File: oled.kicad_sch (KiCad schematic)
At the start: 23 parts, among them Q3 IRLML6402, Q4 BSS138, Q5 BSS138, U7 AP3012KTR-E1

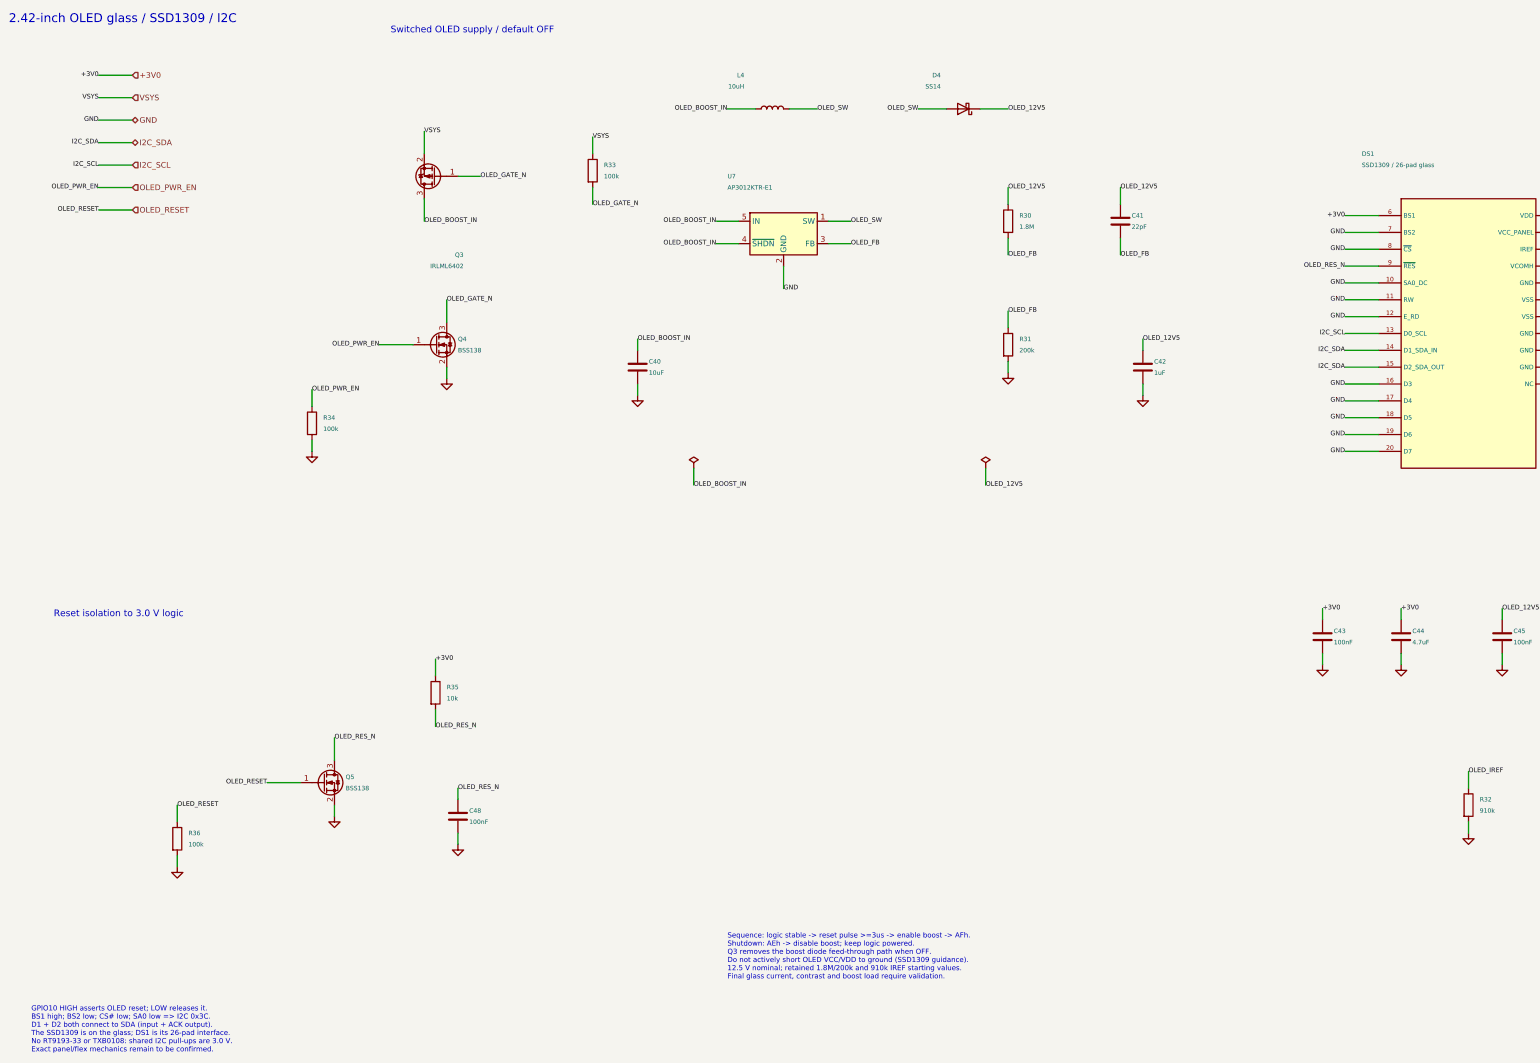
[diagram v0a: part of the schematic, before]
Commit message: Add PCB NFC coil and refine prototype component selections
Integrate a reusable 40 mm four-turn antenna footprint, calculated matching
network, hand-solder tuning pads, and a fabrication-ready bare-coil coupon.
Archive RF calculations, simulation results, reference sources, and tuning
instructions.

Select the PN7160 crystal and supply capacitors using manufacturer guidance
and DC-bias data. Record the confirmed 26-contact OLED interface and dedicated
5 V / 1.5 A USB-C source, retaining the JST-PH battery connector and deferred
battery behavior. Update the BOM, schematic PDFs, and verification tools.

Validation: native KiCad ERC reports zero violations; all current schematic
hashes match the verification report. Coil geometry, coupon DRC, RF model,
and component calculation results are archived with the design.
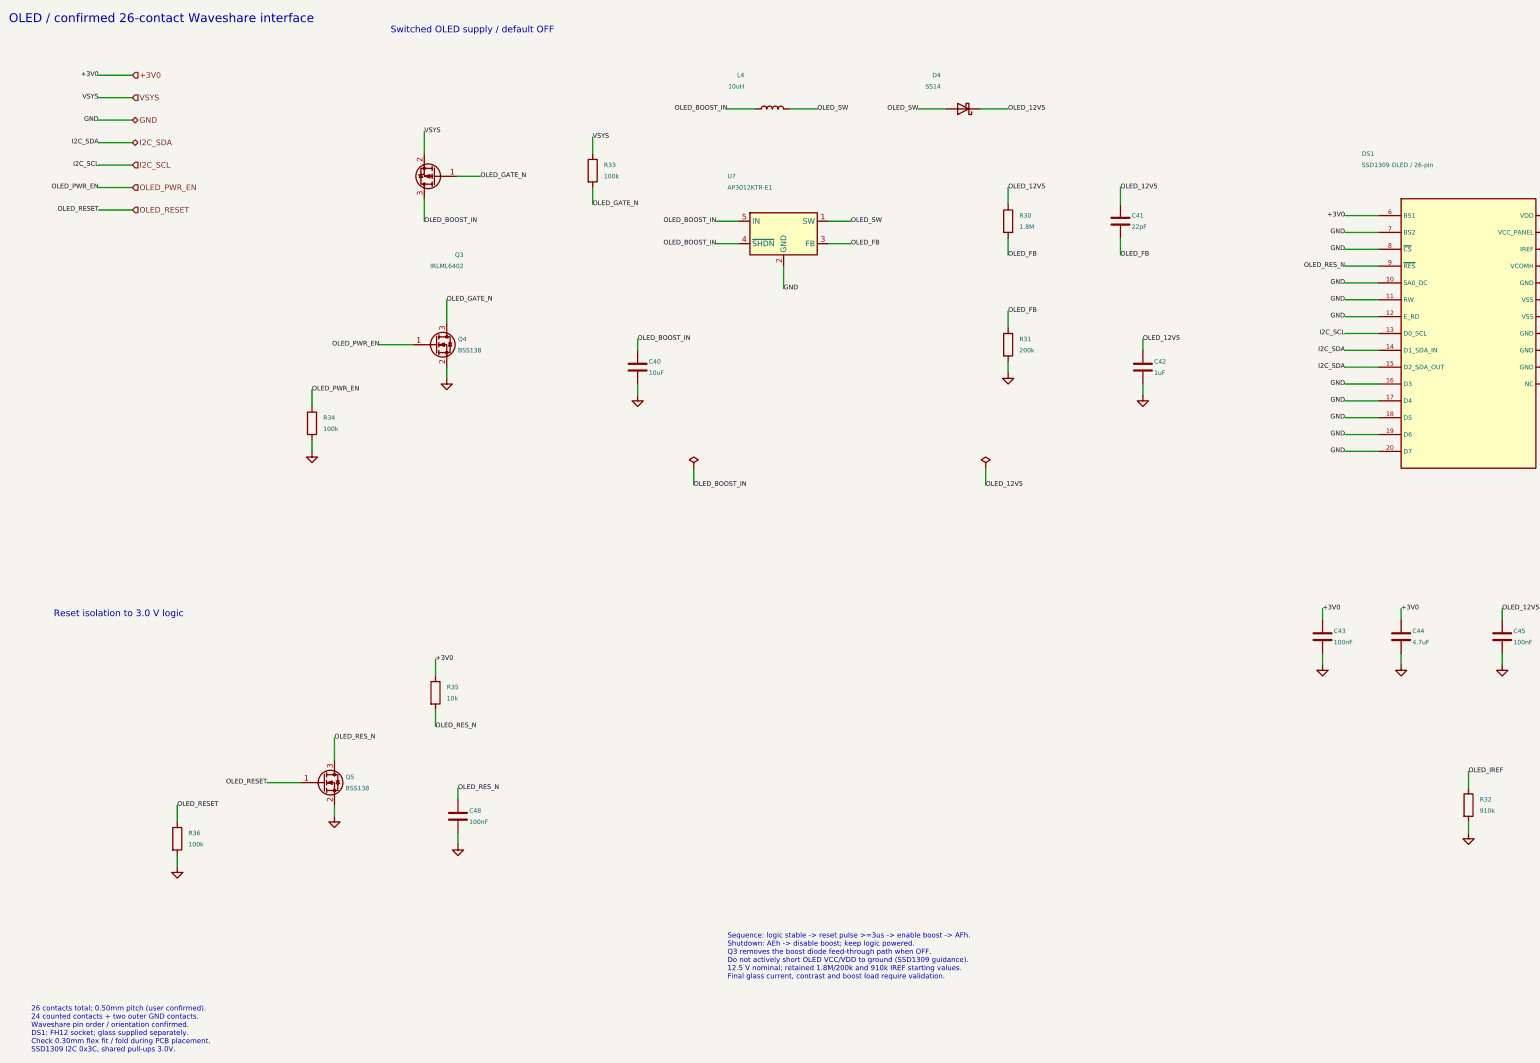
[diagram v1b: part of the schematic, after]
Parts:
- C40: footprint Capacitor_SMD:C_0805_2012Metric -> Capacitor_SMD:C_1206_3216Metric; LCSC (none) -> C14860; MPN (none) -> CL31B106KAHNNNE; Manufacturer (none) -> Samsung Electro-Mechanics; Tolerance 20% -> 10%; Voltage 10 V -> 25 V
- C42: LCSC (none) -> C28323; MPN (none) -> CL21B105KBFNNNE; Manufacturer (none) -> Samsung Electro-Mechanics; Tolerance 20% -> 10%; Voltage 25 V -> 50 V
- C44: LCSC (none) -> C98195; MPN (none) -> CL21B475KAFNNNE; Manufacturer (none) -> Samsung Electro-Mechanics; Tolerance 20% -> 10%; Voltage 10 V -> 25 V
- C46: footprint Capacitor_SMD:C_0805_2012Metric -> Capacitor_SMD:C_1206_3216Metric; LCSC (none) -> C51205; MPN (none) -> CL31B475KBHNNNE; Manufacturer (none) -> Samsung Electro-Mechanics; Tolerance 20% -> 10%; Voltage 25 V -> 50 V
- C47: LCSC (none) -> C19110; MPN (none) -> CL21B225KAFNNNE; Manufacturer (none) -> Samsung Electro-Mechanics; Tolerance 20% -> 10%
- DS1: value SSD1309 / 26-pad glass -> SSD1309 OLED / 26-pin; Actual Flex (none) -> 26 contacts total: 24 counted plus two outer GND contacts; 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; Connector Datasheet (none) -> https://www.hirose.com/product/p/CL0586-0576-2-55; Connector Mechanics (none) -> FH12 bottom-contact, 0.30 mm flex thickness; check insertio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; Footprint Status PROVISIONAL: confirm 26-pin 0.5 mm flex/contact side; may r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 -> SELECTED: 26-way 0.50 mm; user confirms Waveshare pin order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; MPN TBD exact OLED glass -> FH12-26S-0.5SH(55); Manufacturer (none) -> Hirose; Status (none) -> Pinout/orientation confirmed by user; DS1 BOM part is the F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
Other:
- note added: "26 contacts total; 0.50mm pitch (user confirmed). 24 counted contacts + two outer GND contacts. Waveshare pin order / orientation confirmed. DS1: FH12 socket; glass supplied separately. Check 0.30mm flex fit / fold during PCB placement. SSD1309 I2C 0x3C, shared pull-ups 3.0V."
- note added: "OLED / confirmed 26-contact Waveshare interface"
- note removed: "2.42-inch OLED glass / SSD1309 / I2C"
- note removed: "GPIO10 HIGH asserts OLED reset; LOW releases it. BS1 high; BS2 low; CS# low; SA0 low => I2C 0x3C. D1 + D2 both connect to SDA (input + ACK output). The SSD1309 is on the glass; DS1 is its 26-pad interface. No RT9193-33 or TXB0108: shared I2C pull-ups are 3.0 V. Exact panel/flex mechanics remain to be confirmed."
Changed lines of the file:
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@@
     (rev "B-draft")
   )
-  (text "2.42-inch OLED glass / SSD1309 / I2C"
+  (text "OLED / confirmed 26-contact Waveshare interface"
     (at 15.24 17.78 0)
     (effects
@@
       )
     )
-    (property "Footprint" "Capacitor_SMD:C_0805_2012Metric"
+    (property "Footprint" "Capacitor_SMD:C_1206_3216Metric"
       (at 157.48 96.52 0)
       (effects
@@
       )
     )
-    (property "Datasheet" ""
+    (property "Datasheet" "https://product.samsungsem.com/mlcc/CL31B106KAHNNN.do"
       (at 157.48 96.52 0)
       (effects
@@
       )
     )
-    (property "Voltage" "10 V"
+    (property "Voltage" "25 V"
       (at 157.48 96.52 0)
       (effects
@@
       )
     )
-    (property "Tolerance" "20%"
+    (property "Tolerance" "10%"
       (at 157.48 96.52 0)
       (effects
@@
       )
     )
+    (property "Manufacturer" "Samsung Electro-Mechanics"
+      (at 157.48 96.52 0)
+      (effects
+        (font
+          (size 1.27 1.27)
+        )
+        (hide yes)
+      )
+    )
+    (property "MPN" "CL31B106KAHNNNE"
+      (at 157.48 96.52 0)
+      (effects
+        (font
+          (size 1.27 1.27)
+        )
+        (hide yes)
+      )
+    )
+    (property "LCSC" "C14860"
+      (at 157.48 96.52 0)
+      (effects
+        (font
+          (size 1.27 1.27)
+        )
+        (hide yes)
+      )
+    )
     (pin "1"
     )
@@
       )
     )
-    (property "Datasheet" ""
+    (property "Datasheet" "https://product.samsungsem.com/mlcc/CL21B105KBFNNN.do"
       (at 271.78 96.52 0)
       (effects
@@
       )
     )
-    (property "Voltage" "25 V"
+    (property "Voltage" "50 V"
       (at 271.78 96.52 0)
       (effects
@@
       )
     )
-    (property "Tolerance" "20%"
+    (property "Tolerance" "10%"
       (at 271.78 96.52 0)
       (effects
@@
       )
     )
+    (property "Manufacturer" "Samsung Electro-Mechanics"
+      (at 271.78 96.52 0)
+      (effects
+        (font
+          (size 1.27 1.27)
+        )
+        (hide yes)
+      )
+    )
+    (property "MPN" "CL21B105KBFNNNE"
+      (at 271.78 96.52 0)
+      (effects
+        (font
+          (size 1.27 1.27)
+        )
+        (hide yes)
+      )
+    )
+    (property "LCSC" "C28323"
+      (at 271.78 96.52 0)
+      (effects
+        (font
+          (size 1.27 1.27)
+        )
+        (hide yes)
+      )
+    )
     (pin "1"
     )
@@
       )
     )
-    (property "Value" "SSD1309 / 26-pad glass"
+    (property "Value" "SSD1309 OLED / 26-pin"
       (at 321.31 50.8 0)
       (effects
@@
       )
     )
-    (property "MPN" "TBD exact OLED glass"
+    (property "MPN" "FH12-26S-0.5SH(55)"
       (at 345.44 88.9 0)
       (effects
@@
       )
     )
-    (property "Footprint Status" "PROVISIONAL: confirm 26-pin 0.5 mm flex/contact side; may require solder pads instead"
+    (property "Footprint Status" "SELECTED: 26-way 0.50 mm; user confirms Waveshare pin order/orientation, including outer ground contacts"
       (at 345.44 88.9 0)
       (effects
@@
       )
     )
+    (property "Actual Flex" "26 contacts total: 24 counted plus two outer GND contacts; 0.50 mm pitch; copper on emitting side (user confirmed)"
+      (at 345.44 88.9 0)
+      (effects
+        (font
+          (size 1.27 1.27)
+        )
+        (hide yes)
+      )
+    )
+    (property "Status" "Pinout/orientation confirmed by user; DS1 BOM part is the FPC socket, OLED glass supplied separately"
+      (at 345.44 88.9 0)
+      (effects
+        (font
+          (size 1.27 1.27)
+        )
+        (hide yes)
+      )
+    )
+    (property "Manufacturer" "Hirose"
+      (at 345.44 88.9 0)
+      (effects
+        (font
+          (size 1.27 1.27)
+        )
+        (hide yes)
+      )
+    )
+    (property "Connector Mechanics" "FH12 bottom-contact, 0.30 mm flex thickness; check insertion/fold and physical fit during PCB placement"
+      (at 345.44 88.9 0)
+      (effects
+        (font
+          (size 1.27 1.27)
+        )
+        (hide yes)
+      )
+    )
+    (property "Connector Datasheet" "https://www.hirose.com/product/p/CL0586-0576-2-55"
+      (at 345.44 88.9 0)
+      (effects
+        (font
+          (size 1.27 1.27)
+        )
+        (hide yes)
+      )
+    )
     (pin "6"
     )
@@
       )
     )
-    (property "Datasheet" ""
+    (property "Datasheet" "https://product.samsungsem.com/mlcc/CL21B475KAFNNN.do"
       (at 330.2 157.48 0)
       (effects
@@
       )
     )
-    (property "Voltage" "10 V"
+    (property "Voltage" "25 V"
       (at 330.2 157.48 0)
       (effects
@@
       )
     )
-    (property "Tolerance" "20%"
+    (property "Tolerance" "10%"
       (at 330.2 157.48 0)
       (effects
@@
       )
     )
+    (property "Manufacturer" "Samsung Electro-Mechanics"
+      (at 330.2 157.48 0)
+      (effects
+        (font
+          (size 1.27 1.27)
+        )
+        (hide yes)
+      )
+    )
+    (property "MPN" "CL21B475KAFNNNE"
+      (at 330.2 157.48 0)
+      (effects
+        (font
+          (size 1.27 1.27)
+        )
+        (hide yes)
+      )
+    )
+    (property "LCSC" "C98195"
+      (at 330.2 157.48 0)
+      (effects
+        (font
+          (size 1.27 1.27)
+        )
+        (hide yes)
+      )
+    )
     (pin "1"
     )
@@
       )
     )
-    (property "Footprint" "Capacitor_SMD:C_0805_2012Metric"
+    (property "Footprint" "Capacitor_SMD:C_1206_3216Metric"
       (at 370.84 157.48 0)
       (effects
@@
       )
     )
-    (property "Datasheet" ""
+    (property "Datasheet" "https://product.samsungsem.com/mlcc/CL31B475KBHNNN.do"
       (at 370.84 157.48 0)
       (effects
@@
       )
     )
-    (property "Voltage" "25 V"
+    (property "Voltage" "50 V"
       (at 370.84 157.48 0)
       (effects
@@
       )
     )
-    (property "Tolerance" "20%"
+    (property "Tolerance" "10%"
       (at 370.84 157.48 0)
       (effects
@@
       )
     )
+    (property "Manufacturer" "Samsung Electro-Mechanics"
+      (at 370.84 157.48 0)
+      (effects
+        (font
+          (size 1.27 1.27)
+        )
+        (hide yes)
+      )
+    )
+    (property "MPN" "CL31B475KBHNNNE"
+      (at 370.84 157.48 0)
+      (effects
+        (font
+          (size 1.27 1.27)
+        )
+        (hide yes)
+      )
+    )
+    (property "LCSC" "C51205"
+      (at 370.84 157.48 0)
+      (effects
+        (font
+          (size 1.27 1.27)
+        )
+        (hide yes)
+      )
+    )
     (pin "1"
     )
@@
       )
     )
-    (property "Datasheet" ""
+    (property "Datasheet" "https://product.samsungsem.com/mlcc/CL21B225KAFNNN.do"
       (at 391.16 157.48 0)
       (effects
@@
       )
     )
-    (property "Tolerance" "20%"
+    (property "Tolerance" "10%"
       (at 391.16 157.48 0)
       (effects
@@
       )
     )
+    (property "Manufacturer" "Samsung Electro-Mechanics"
+      (at 391.16 157.48 0)
+      (effects
+        (font
+          (size 1.27 1.27)
+        )
+        (hide yes)
+      )
+    )
+    (property "MPN" "CL21B225KAFNNNE"
+      (at 391.16 157.48 0)
+      (effects
+        (font
+          (size 1.27 1.27)
+        )
+        (hide yes)
+      )
+    )
+    (property "LCSC" "C19110"
+      (at 391.16 157.48 0)
+      (effects
+        (font
+          (size 1.27 1.27)
+        )
+        (hide yes)
+      )
+    )
     (pin "1"
     )
@@
     )
   )
-  (text "GPIO10 HIGH asserts OLED reset; LOW releases it.\nBS1 high; BS2 low; CS# low; SA0 low => I2C 0x3C.\nD1 + D2 both connect to SDA (input + ACK output).\nThe SSD1309 is on the glass; DS1 is its 26-pad interface.\nNo RT9193-33 or TXB0108: shared I2C pull-ups are 3.0 V.\nExact panel/flex mechanics remain to be confirmed."
+  (text "26 contacts total; 0.50mm pitch (user confirmed).\n24 counted contacts + two outer GND contacts.\nWaveshare pin order / orientation confirmed.\nDS1: FH12 socket; glass supplied separately.\nCheck 0.30mm flex fit / fold during PCB placement.\nSSD1309 I2C 0x3C, shared pull-ups 3.0V."
     (at 20.32 246.38 0)
     (effects

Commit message: Prepare components and JLCPCB BOM for 10-board assembly
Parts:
- C41: LCSC (none) -> C1653; MPN (none) -> CL10C220JB8NNNC; Manufacturer (none) -> Samsung Electro-Mechanics; Tolerance 10% -> 5%
- C43, C48: LCSC (none) -> C1591; MPN (none) -> CL10B104KB8NNNC; Manufacturer (none) -> Samsung Electro-Mechanics; Voltage 10 V -> 50 V
- C45: LCSC (none) -> C1591; MPN (none) -> CL10B104KB8NNNC; Manufacturer (none) -> Samsung Electro-Mechanics; Voltage 25 V -> 50 V
- D4: LCSC (none) -> C47460; Manufacturer Vishay -> Vishay Intertech
- DS1: LCSC (none) -> C202113; Manufacturer Hirose -> HRS(Hirose); Panel Datasheet (none) -> https://files.waveshare.com/wiki/2.42inch-OLED-Module/SSD13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
- L4: LCSC (none) -> C6127589
- Q3: LCSC (none) -> C2593; Manufacturer (none) -> Infineon Technologies
- Q4, Q5: LCSC (none) -> C52895
- R30: footprint Resistor_SMD:R_0603_1608Metric -> Resistor_SMD:R_0805_2012Metric; LCSC (none) -> C2088132; MPN (none) -> CPF0805B1M8E; Manufacturer (none) -> TE Connectivity; Rating 0.1 W -> 0.1 W; 100 V; 25 ppm/K
- R31: LCSC (none) -> C728585; MPN (none) -> RT0603BRD07200KL; Manufacturer (none) -> YAGEO
- R32: LCSC (none) -> C23263; MPN (none) -> 0603WAF9103T5E; Manufacturer (none) -> UNI-ROYAL(Uniroyal Elec)
- R33, R34, R36: LCSC (none) -> C25803; MPN (none) -> 0603WAF1003T5E; Manufacturer (none) -> UNI-ROYAL(Uniroyal Elec)
- R35: LCSC (none) -> C25804; MPN (none) -> 0603WAF1002T5E; Manufacturer (none) -> UNI-ROYAL(Uniroyal Elec)
- U7: LCSC (none) -> C460356
